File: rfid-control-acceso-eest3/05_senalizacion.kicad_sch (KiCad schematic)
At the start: 8 parts, among them Q1 NMOS_3V3?

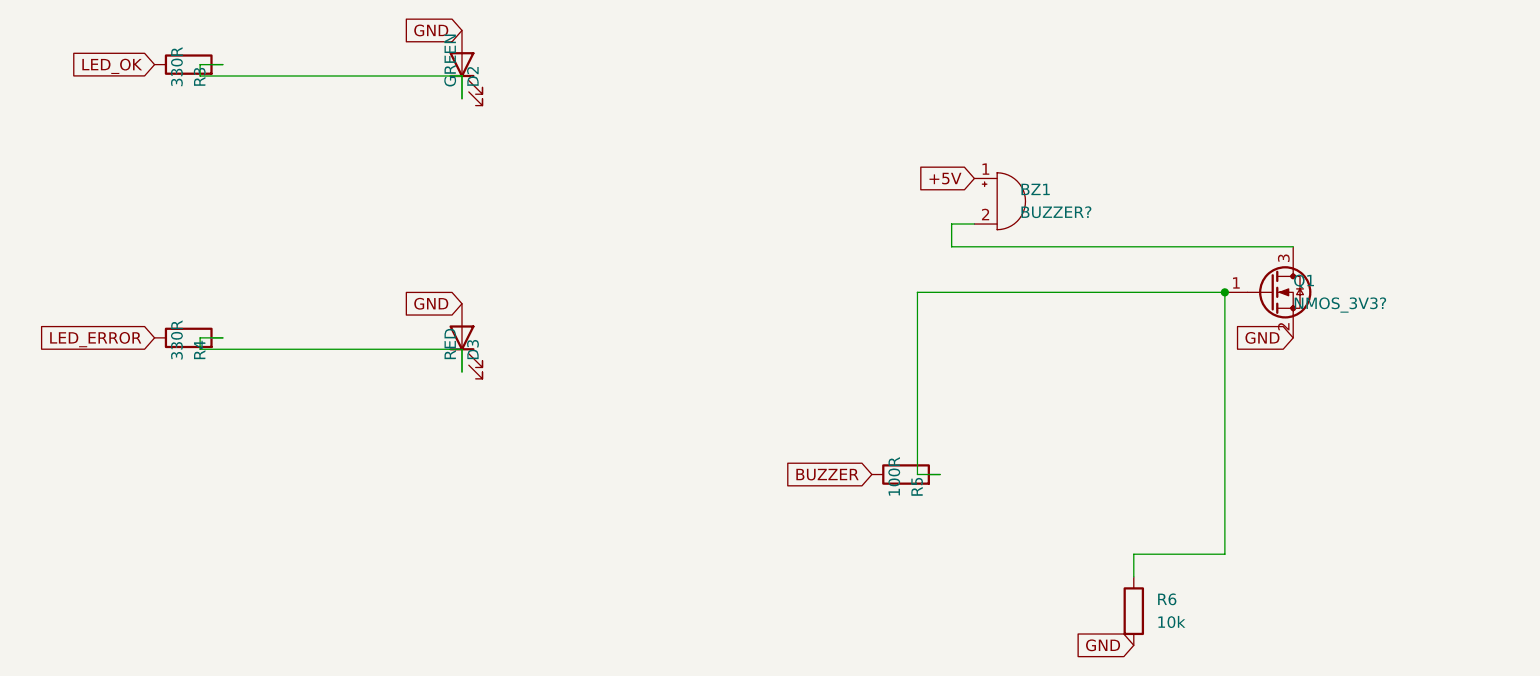
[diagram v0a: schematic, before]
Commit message: Reorganiza floorplan PCB Rev A antes del ruteo
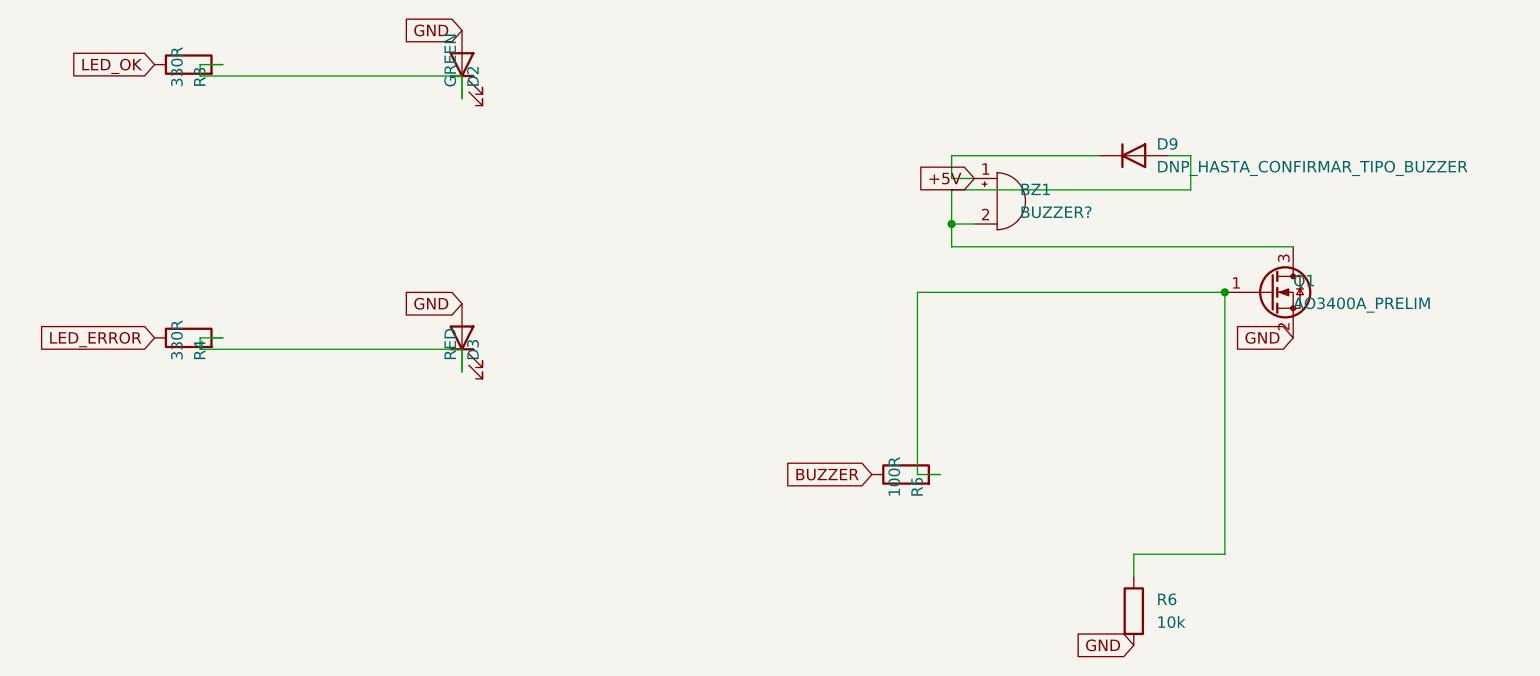
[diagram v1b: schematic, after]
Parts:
- added D9: DNP_HASTA_CONFIRMAR_TIPO_BUZZER, Diode_THT:D_DO-35_SOD27_P10.16mm_Horizontal, symbol Device:D
- BZ1: footprint (none) -> Buzzer_Beeper:Buzzer_12x9.5RM7.6
- D2, D3: footprint (none) -> LED_THT:LED_D5.0mm
- Q1: value NMOS_3V3? -> AO3400A_PRELIM; footprint (none) -> Package_TO_SOT_SMD:SOT-23; Pinout_Verified (none) -> AO3400A AOS: 1=G, 2=S, 3=D
- R3, R4, R5, R6: footprint (none) -> Resistor_THT:R_Axial_DIN0207_L6.3mm_D2.5mm_P10.16mm_Horizontal
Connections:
- net +5V: now also D9.1 (K)
- net at BZ1.2 (-), Q1.3 (D): now also D9.2 (A)
